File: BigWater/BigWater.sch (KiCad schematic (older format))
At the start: 60 parts, among them J1 Conn_01x19, J2 Conn_01x19, J3 ADS1115, J4 Conn_01x02, U1 LM7805_TO220

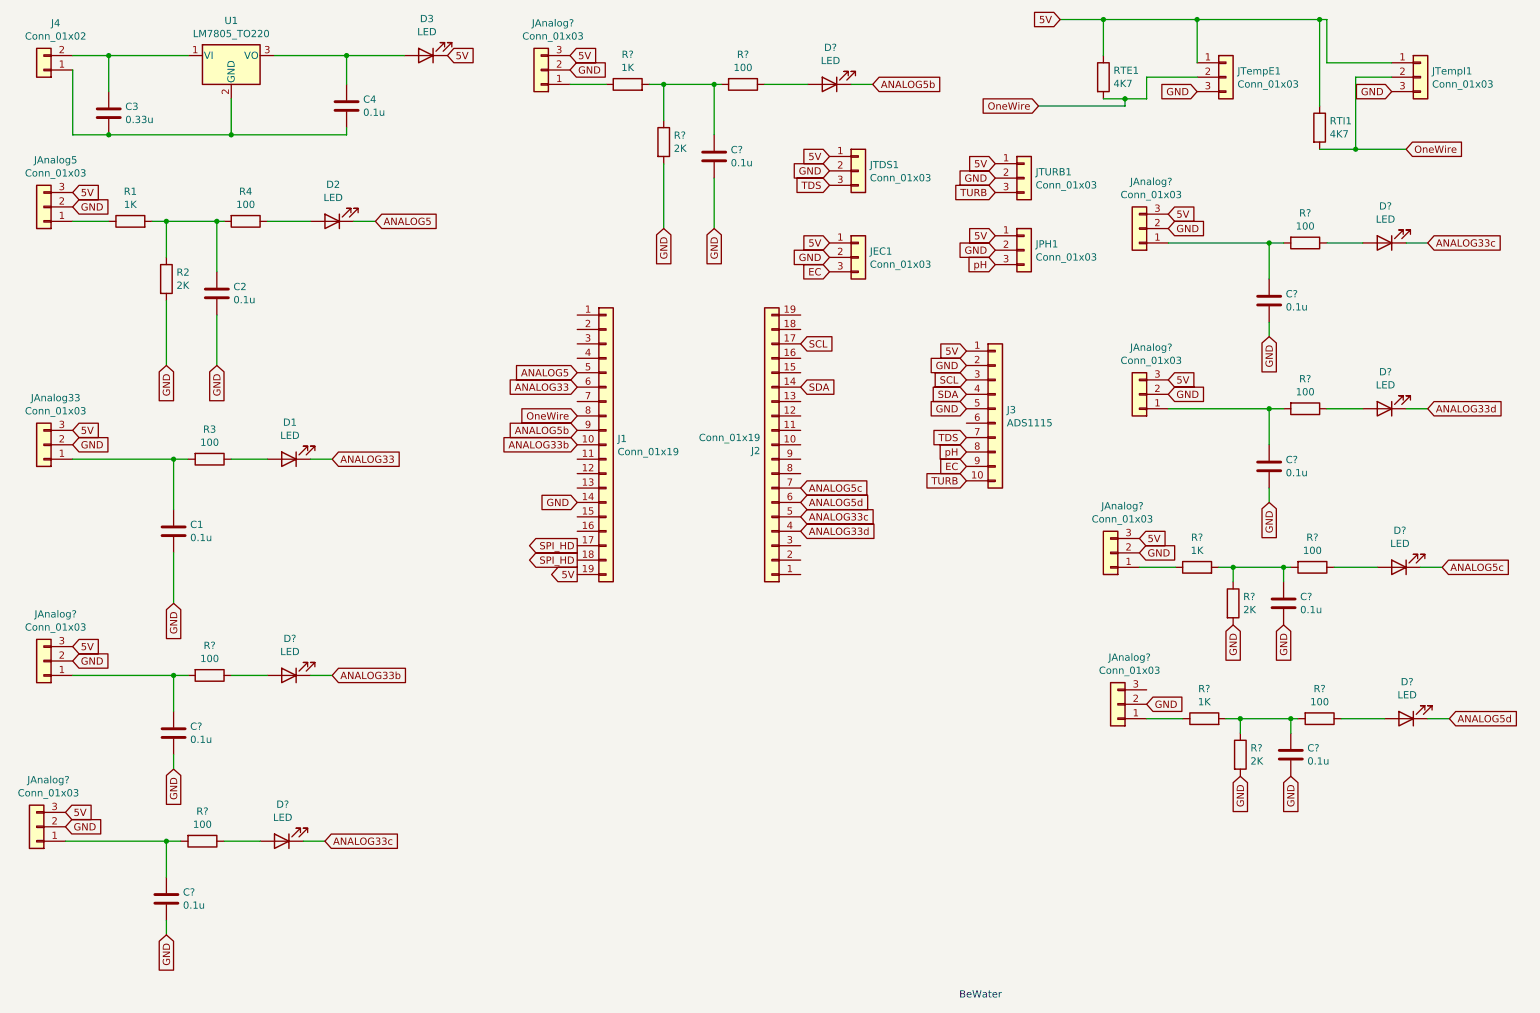
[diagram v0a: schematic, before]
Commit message: Añadido diseño de la PCB
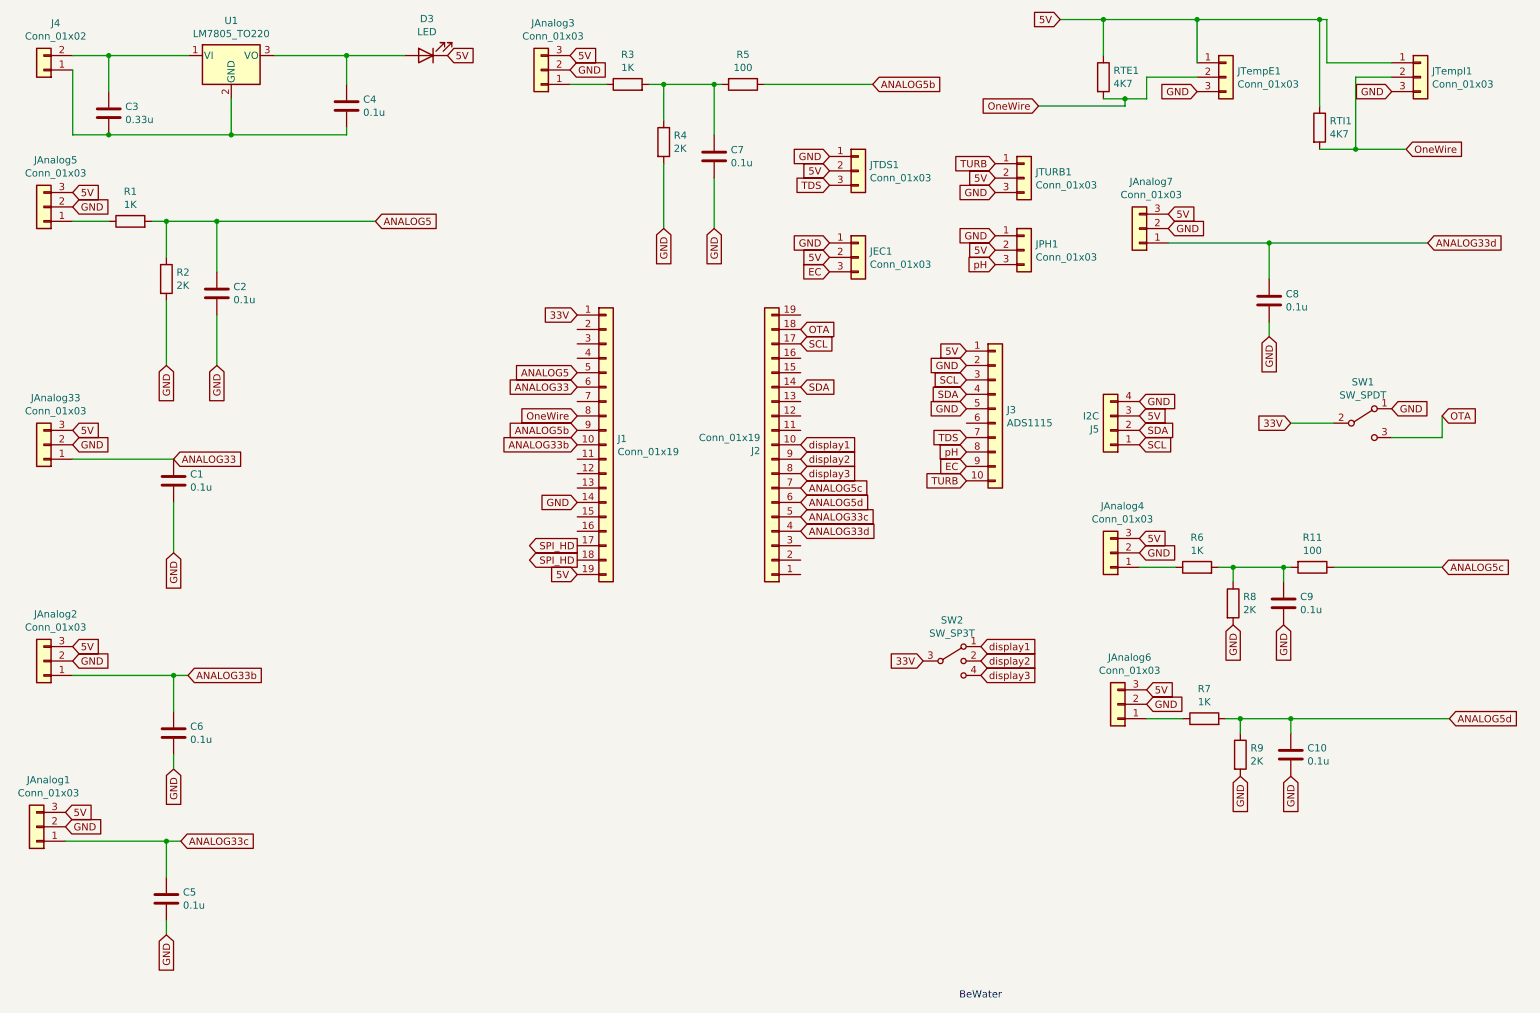
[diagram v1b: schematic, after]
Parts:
- removed C?: 0.1u, symbol Device:C
- removed D1, D2, D? (x7): LED, symbol Device:LED
- removed JAnalog?: Conn_01x03, symbol Connector_Generic:Conn_01x03
- removed R3, R4, R? (x5): 100, symbol Device:R
- added J5: I2C, Connector_PinSocket_2.54mm:PinSocket_1x04_P2.54mm_Vertical, symbol Connector_Generic:Conn_01x04
- added SW1: SW_SPDT, Button_Switch_SMD:SW_DIP_SPSTx01_Slide_Copal_CVS-01xB_W5.9mm_P1mm, symbol Switch:SW_SPDT
- added SW2: SW_SP3T, Button_Switch_SMD:SW_SP3T_PCM13, symbol Switch:SW_SP3T
- C1, C2, C3, C4: footprint (none) -> Capacitor_THT:C_Disc_D3.0mm_W2.0mm_P2.50mm
- C10, C5, C6, C7, C8, C9: renamed from C?; footprint (none) -> Capacitor_THT:C_Disc_D3.0mm_W2.0mm_P2.50mm
- D3: footprint (none) -> LED_THT:LED_D5.0mm
- J1, J2: footprint (none) -> Connector_PinSocket_2.54mm:PinSocket_1x19_P2.54mm_Vertical
- J3: footprint (none) -> Connector_PinSocket_2.54mm:PinSocket_1x10_P2.54mm_Vertical
- J4: footprint (none) -> TerminalBlock:TerminalBlock_bornier-2_P5.08mm
- JAnalog1, JAnalog2, JAnalog3, JAnalog4, JAnalog6, JAnalog7: renamed from JAnalog?; footprint (none) -> Connector_PinSocket_2.54mm:PinSocket_1x03_P2.54mm_Vertical
- JAnalog33, JAnalog5: footprint (none) -> Connector_PinSocket_2.54mm:PinSocket_1x03_P2.54mm_Vertical
- JEC1, JPH1, JTDS1, JTURB1, JTempE1, JTempI1: footprint (none) -> Connector_JST:JST_EH_B3B-EH-A_1x03_P2.50mm_Vertical
- R1, R2, RTE1, RTI1: footprint (none) -> Resistor_THT:R_Axial_DIN0207_L6.3mm_D2.5mm_P7.62mm_Horizontal
- R11, R3, R4, R5, R6, R7, R8, R9: renamed from R?; footprint (none) -> Resistor_THT:R_Axial_DIN0207_L6.3mm_D2.5mm_P7.62mm_Horizontal
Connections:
- net 5V: now also JAnalog6.3 (Pin_3), JEC1.2 (Pin_2), JPH1.2 (Pin_2), JTDS1.2 (Pin_2), JTURB1.2 (Pin_2), J5.3 (Pin_3); no longer JEC1.1 (Pin_1), JPH1.1 (Pin_1), JTDS1.1 (Pin_1), JTURB1.1 (Pin_1)
- net ANALOG33: now also C1.1, JAnalog33.1 (Pin_1)
- net ANALOG33b: now also C6.1, JAnalog2.1 (Pin_1)
- net ANALOG33c: now also C5.1, JAnalog1.1 (Pin_1)
- net ANALOG33d: now also C8.1, JAnalog7.1 (Pin_1)
- net ANALOG5: now also C2.1, R1.2, R2.1
- net ANALOG5b: now also R5.1
- net ANALOG5c: now also R11.1
- net ANALOG5d: now also C10.1, R7.2, R9.1
- net GND: now also JEC1.1 (Pin_1), JPH1.1 (Pin_1), JTDS1.1 (Pin_1), JTURB1.3 (Pin_3), J5.4 (Pin_4), SW1.1 (A); no longer JEC1.2 (Pin_2), JPH1.2 (Pin_2), JTDS1.2 (Pin_2), JTURB1.2 (Pin_2)
- net SCL: now also J5.1 (Pin_1)
- net SDA: now also J5.2 (Pin_2)
- net TURB: now also JTURB1.1 (Pin_1); no longer JTURB1.3 (Pin_3)
- net 33V: now reaches J1.1 (Pin_1)
- net 33V: now also SW1.2 (B), SW2.3
- net display1: now reaches J2.10 (Pin_10)
- net display1: now also SW2.1
- net OTA: now reaches J2.18 (Pin_18)
- net OTA: now also SW1.3 (C)
- net display3: now reaches J2.8 (Pin_8)
- net display3: now also SW2.4
- net display2: now reaches J2.9 (Pin_9)
- net display2: now also SW2.2
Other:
- moved on the sheet: C1
